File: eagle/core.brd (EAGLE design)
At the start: 45.7 x 17.8 mm, 20 parts

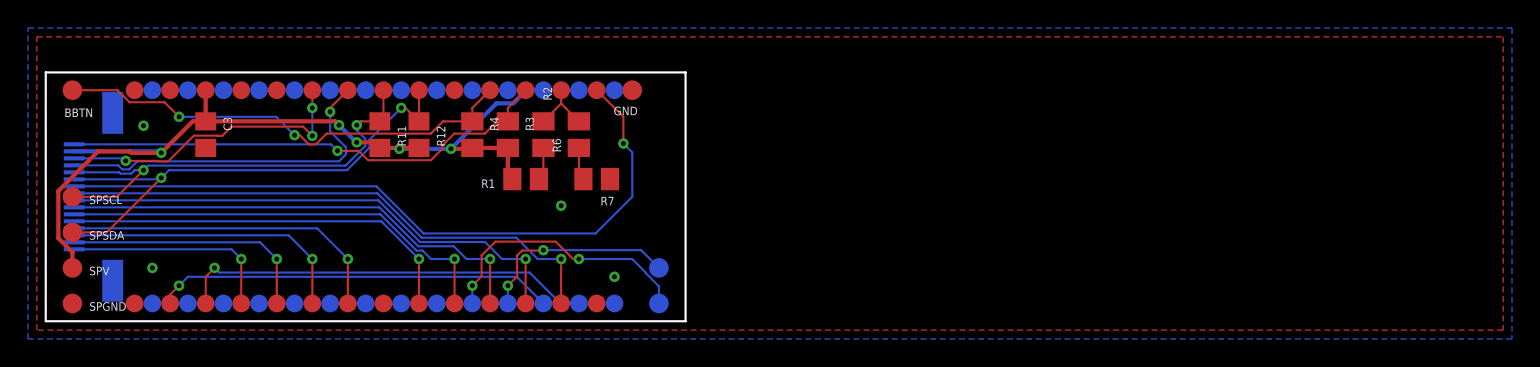
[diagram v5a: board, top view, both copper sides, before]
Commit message: Added altimeter code
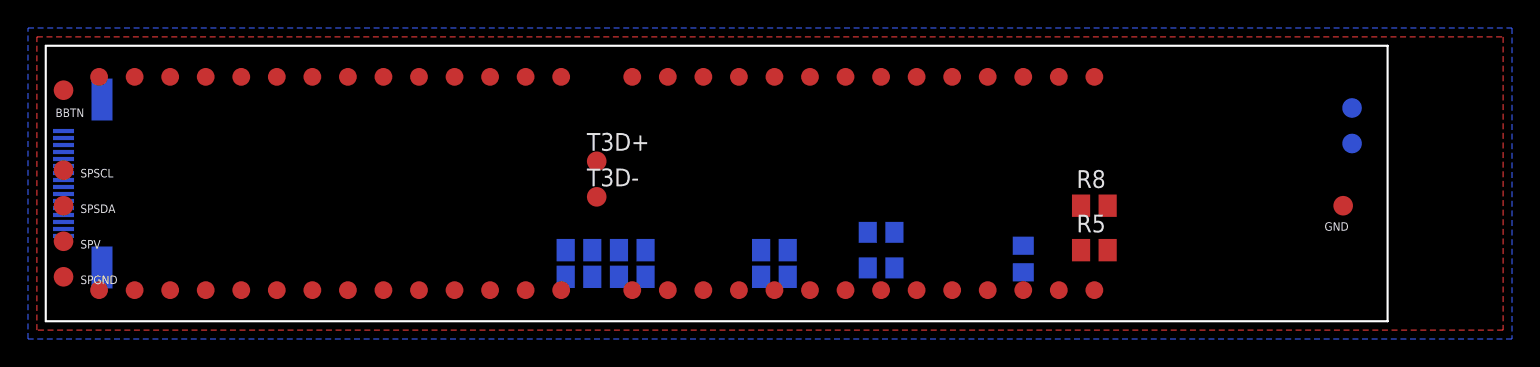
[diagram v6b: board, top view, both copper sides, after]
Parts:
- added R5, R8: 10k, resistor:M0805
- added T3D+, T3D-: TPTP14R, testpad:TP14R
- moved C3 59.1 mm to (69.8, 4.45), flipped to the bottom, turned to 90 degrees
- moved GND 51.5 mm to (92.7, 8.26)
- moved ENCL 50.8 mm to (93.3, 15.2)
- moved ENCR 50.8 mm to (93.3, 12.7)
- moved U$1 38.1 mm to (59.7, 9.84), turned to 180 degrees
- moved R11 37.1 mm to (59.7, 3.81), flipped to the bottom, turned to 180 degrees
- moved R12 33.8 mm to (59.7, 6.35), flipped to the bottom, turned to 180 degrees
- moved R4 23.9 mm to (52.1, 3.17), flipped to the bottom, turned to 180 degrees
- moved R3 20.8 mm to (52.1, 5.08), flipped to the bottom, turned to 180 degrees
- moved R2 12.0 mm to (41.9, 3.17), flipped to the bottom, turned to 0 degrees
- moved R6 9.09 mm to (41.9, 5.08), flipped to the bottom, turned to 180 degrees
- moved R1 7.96 mm to (38.1, 3.17), flipped to the bottom, turned to 0 degrees
- moved R7 5.24 mm to (38.1, 5.08), flipped to the bottom
- moved U$2 3.93 mm to (21.6, 9.84), flipped to the top, turned to 180 degrees
- moved SPSDA 2.01 mm to (1.27, 8.26)
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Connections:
- new net 4VREAD: R5.1, R8.2, U$1.17
- net 4V: now also R5.2
- net ANTPIN: now also U$1.22; no longer U$1.14
- net GND: now also R8.1, U$1.GND1
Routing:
- net 3V: track 61.6 -> 0.00 mm, vias 5 -> 0
- net SCK: track 51.0 -> 0.00 mm, vias 1 -> 0
- net MOSI: track 39.9 -> 0.00 mm, vias 1 -> 0
- net SDA: track 37.7 -> 0.00 mm, vias 2 -> 0
- net TFTCS: track 37.2 -> 0.00 mm, vias 1 -> 0
- net PBTN: track 35.5 -> 0.00 mm, vias 1 -> 0
- net DC: track 34.4 -> 0.00 mm, vias 1 -> 0
- net BBTN: track 33.6 -> 0.00 mm, vias 2 -> 0
- net SCL: track 33.4 -> 0.00 mm, vias 2 -> 0
- net DOUT: track 31.7 -> 0.00 mm, vias 1 -> 0
- net T4TX: track 29.9 -> 0.00 mm, vias 1 -> 0
- net TFTRST: track 28.9 -> 0.00 mm, vias 1 -> 0
- net T4RX: track 28.6 -> 0.00 mm, vias 1 -> 0
- net LRCL: track 25.6 -> 0.00 mm, vias 1 -> 0
- net L4-: track 23.6 -> 0.00 mm, vias 1 -> 0
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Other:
- board size 45.7 x 17.8 mm -> 95.9 x 19.7 mm
